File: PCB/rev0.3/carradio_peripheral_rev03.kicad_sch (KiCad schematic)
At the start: 258 parts, among them J1 ISO 10487 A (via pigtail), J10 Expansion, J11 SMA GNSS antenna, J12 Display buttons, J13 HDMI in (from VIM3), J14 Display FPC 40P 0.5mm, J17 RTL-SDR (internal), J18 VIM3 VIN (JST-XH 2P), J19 External USB 1, J2 VIM3 40-pin via 2x20 IDC ribb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, J20 External USB 2, J21 Expansion 2, J22 SWD, J5 VIM3 POWER key lead, J7 BH1750 light sensor, J8 ISO 10487 C1 (via pigtail), Q1 AO3400A, Q10 P-MOSFET -40V, Q11 CSD18543Q3A, Q12 CSD18543Q3A, Q2 P-MOSFET -60V, Q3 2N7002, SW1 BOOTSEL, SW2 RESET, U1 TPS560430XDBVR, U10 PCM5102APWR, U11 PCM5102APWR, U12 TPS55288RPMR, U13 CH334R, U14 CH334R, U15 LMR33630ADDA, U16 TPS2561DRCR, U17 USBLC6-2SC6, U18 USBLC6-2SC6, U19 AP2112K-3.3, U2 EL817S1(C), U20 RP2350B, U21 W25Q128JVS, U3 EL817S1(C), U4 EL817S1(C), U5 EL817S1(C), U6 LP5907MFX-3.3, U7 NEO-M9N-00B, U8 LP5907MFX-3.3, U9 LP5907MFX-3.3, Y1 12MHz, Y2 12MHz, Y3 12MHz

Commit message: PCB rev 0.3: KiCad import notes, TL3342 footprint for SW1/SW2
Checked every footprint name against the KiCad libraries and wrote down
the three parts that still need a footprint (TPS55288, fuse holder,
XUNPU FPC) and how to get them.

Co-Authored-By: Claude Opus 5.5 (1M context) <noreply@anthropic.com>
Claude-Session: https://claude.ai/code/session_01C8m2AkFwQrNE2yN9Ymgjwu
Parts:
- SW1, SW2: footprint (none) -> Button_Switch_SMD:SW_SPST_TL3342; MPN E-Switch TL3342F160QG (use the LCSC footprint; LCSC lists 5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 -> E-Switch TL3342F160QG
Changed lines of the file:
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@@
     (property
       "Footprint"
-      ""
+      "Button_Switch_SMD:SW_SPST_TL3342"
       (at 940 290 0)
       (effects
@@
     (property
       "MPN"
-      "E-Switch TL3342F160QG (use the LCSC footprint; LCSC lists 5.2x5.2mm)"
+      "E-Switch TL3342F160QG"
       (at 940 290 0)
       (effects
@@
     (property
       "Footprint"
-      ""
+      "Button_Switch_SMD:SW_SPST_TL3342"
       (at 1110 100 0)
       (effects
@@
     (property
       "MPN"
-      "E-Switch TL3342F160QG (use the LCSC footprint; LCSC lists 5.2x5.2mm)"
+      "E-Switch TL3342F160QG"
       (at 1110 100 0)
       (effects

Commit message: PCB rev 0.2/0.3: fix KiCad 10 footprint pad mismatches
- J13 HDMI footprint lives in Connector_Video, not Connector_HDMI
- USB-A shield pin renumbered SH to match the Molex 67643 footprint
- Hub crystals Y1/Y2 use Crystal_GND24 (pads 2/4 to GND)
- J14 FPC mounting pads (MP) tied to GND

Co-Authored-By: Claude Opus 5.5 (1M context) <noreply@anthropic.com>
Claude-Session: https://claude.ai/code/session_01C8m2AkFwQrNE2yN9Ymgjwu
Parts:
- removed J14: Display FPC 40P 0.5mm, Connector_FFC-FPC:Hirose_FH12-40S-0.5SH_1x40-1MP_P0.50mm_Horizontal, symbol Connector_Generic:Conn_01x40
- removed R84: 27Ω, Resistor_SMD:R_0603_1608Metric, symbol Device:R
- removed R87, R88, R89: 10k, Resistor_SMD:R_0603_1608Metric, symbol Device:R
- removed U19: AP2112K-3.3, Package_TO_SOT_SMD:SOT-23-5, symbol Regulator_Linear:AP2112K-3.3
- removed Y1, Y2: 12MHz, Crystal:Crystal_SMD_3225-4Pin_3.2x2.5mm, symbol Device:Crystal
- added C61: 1uF, Capacitor_SMD:C_0603_1608Metric, symbol Device:C
- added C81: 10uF, Capacitor_SMD:C_0805_2012Metric, symbol Device:C
- added J14: Display FPC 40P 0.5mm, Connector_FFC-FPC:Hirose_FH12-40S-0.5SH_1x40-1MP_P0.50mm_Horizontal, symbol Connector_Generic_MountingPin:Conn_01x40_MountingPin
- added J19: External USB 1, Connector_USB:USB_A_Molex_67643_Horizontal, symbol Connector:USB_A
- added R79: 1k, Resistor_SMD:R_0603_1608Metric, symbol Device:R
- added R85, R91, R92: 10k, Resistor_SMD:R_0603_1608Metric, symbol Device:R
- C76: renamed from J19; value External USB 1 -> 10uF; footprint Connector_USB:USB_A_Molex_67643_Horizontal -> Capacitor_SMD:C_0805_2012Metric; symbol Connector:USB_A -> Device:C; LCSC C2798029 -> C15850; MPN Molex 67643-0910 USB-A -> 0805 10uF 25V X5R
- J13: footprint Connector_HDMI:HDMI_A_Amphenol_10029449-x01xLF_Horizontal -> Connector_Video:HDMI_A_Amphenol_10029449-x01xLF_Horizontal
- R84: renamed from R85; value 10k -> 27Ω; LCSC C25804 -> C25190; MPN 0603 10k 1% -> UNI-ROYAL 0603WAF270JT5E 27R
- R87: renamed from R90; value 1k -> 10k; LCSC C21190 -> C25804; MPN 0603 1k 1% -> 0603 10k 1%
- R88: renamed from R79; value 1k -> 10k; LCSC C21190 -> C25804; MPN 0603 1k 1% -> 0603 10k 1%
- R90: renamed from R92; value 10k -> 1k; LCSC C25804 -> C21190; MPN 0603 10k 1% -> 0603 1k 1%
- U19: renamed from C81; value 10uF -> AP2112K-3.3; footprint Capacitor_SMD:C_0805_2012Metric -> Package_TO_SOT_SMD:SOT-23-5; symbol Device:C -> Regulator_Linear:AP2112K-3.3; LCSC C15850 -> C51118; MPN 0805 10uF 25V X5R -> Diodes AP2112K-3.3TRG1
- Y1: renamed from C61; value 1uF -> 12MHz; footprint Capacitor_SMD:C_0603_1608Metric -> Crystal:Crystal_SMD_3225-4Pin_3.2x2.5mm; symbol Device:C -> Device:Crystal_GND24; LCSC C77386 -> C9002; MPN 0603 1uF 50V X5R (Murata GRM188R61H105KAALD) -> YXC X322512MSB4SI 12MHz
- Y2: renamed from C76; value 10uF -> 12MHz; footprint Capacitor_SMD:C_0805_2012Metric -> Crystal:Crystal_SMD_3225-4Pin_3.2x2.5mm; symbol Device:C -> Device:Crystal_GND24; LCSC C15850 -> C9002; MPN 0805 10uF 25V X5R -> YXC X322512MSB4SI 12MHz
- renumbered R91 to R89
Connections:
- net +3V3_MCU: now also R87.1, R88.1, R89.1, U19.5 (VOUT), C81.1, R85.1; no longer R84.1, U19.1
- net +5V_AON: now also U19.1 (VIN), U19.3 (EN)
- net +5V_SYS: now also C61.1, J14.4 (Pin_4), J14.5 (Pin_5), J14.6 (Pin_6), R91.1; no longer R89.1, Y1.1
- net BL_EN: now also J14.37 (Pin_37)
- net BL_PWM: now also J14.36 (Pin_36)
- net EXT1_DM: now also J19.2 (D-); no longer C76.2 (D-)
- net EXT1_DP: now also J19.3 (D+); no longer C76.3 (D+)
- net EXT1_VBUS: now also J19.1 (VBUS); no longer C76.1 (VBUS)
- net GND: now also C76.2, J17.SH (Shield), J20.SH (Shield), Y1.4, Y2.4, C61.2, C81.2, J14.10 (Pin_10), J14.12 (Pin_12), J14.15 (Pin_15), J14.18 (Pin_18), J14.21 (Pin_21), J14.26 (Pin_26), J14.35 (Pin_35), J14.8 (Pin_8), J14.9 (Pin_9), J14.MP (MountPin), J19.4 (GND), J19.SH (Shield), R92.2; no longer C76.4 (GND), C76.5 (Shield), J17.5 (Shield), J20.5 (Shield), R90.2
- net GNSS_SAFEBOOT: now also R79.2; no longer R88.2
- net HDMI_5V: now also J14.27 (Pin_27)
- net HDMI_CEC: now also J14.23 (Pin_23)
- net HDMI_CLKN: now also J14.22 (Pin_22)
- net HDMI_CLKP: now also J14.20 (Pin_20)
- net HDMI_D0N: now also J14.19 (Pin_19)
- net HDMI_D0P: now also J14.17 (Pin_17)
- net HDMI_D1N: now also J14.16 (Pin_16)
- net HDMI_D1P: now also J14.14 (Pin_14)
- net HDMI_D2N: now also J14.13 (Pin_13)
- net HDMI_D2P: now also J14.11 (Pin_11)
- net HDMI_HPD: now also J14.28 (Pin_28)
- net HDMI_SCL: now also J14.24 (Pin_24)
- net HDMI_SDA: now also J14.25 (Pin_25)
- net HUB1_RST: now also R90.2; no longer R87.2
- net HUB2_3V3: now also C76.1; no longer Y2.1
- net HUB2_XI: now also Y2.1
- net HUB2_XO: now also Y2.3
- net HUB_XI: now also Y1.1
- net HUB_XO: now also Y1.3
- net MCU_5VSYS_ADC: now also R91.2, R92.1; no longer R89.2, R90.1
- net MCU_GNSS_SAFEBOOT: now also R79.1; no longer R88.1
- net MCU_HUB_RST: now also R90.1; no longer R87.1
- net MCU_RUN: now also R85.2; no longer R84.2
- net MCU_USBP_FAULT1: now also R87.2
- net MCU_USBP_FAULT2: now also R88.2
- net MCU_USBP_PG: now also R89.2
- net MCU_USB_DP: now also R84.2
- net MCU_USB_DP_R: now also R84.1
- net TOUCH_DN: now also J14.34 (Pin_34)
- net TOUCH_DP: now also J14.33 (Pin_33)
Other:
- moved on the sheet: R84, R87, R88, R89, R90

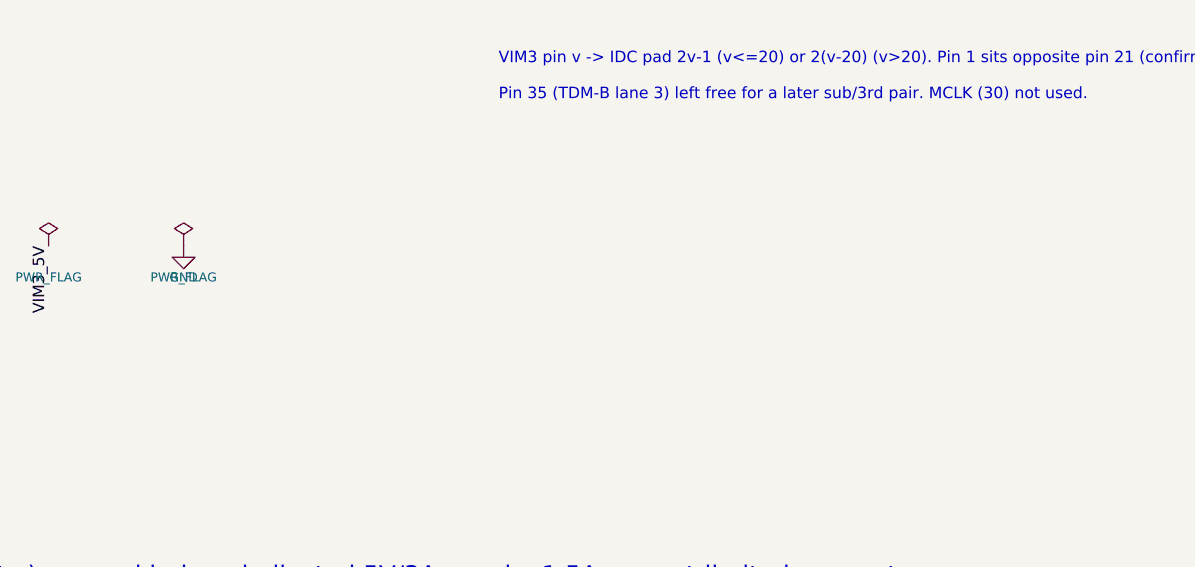
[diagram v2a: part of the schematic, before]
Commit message: PCB rev 0.3: board placement, HDMI routing, LCSC footprints
- carradio_peripheral_rev03.kicad_pcb: 109 x 92 mm, 4 layers (In1 GND plane),
  all 258 parts placed, 40-pin VIM3 header on the top edge
- HDMI socket -> display FPC routed; all 8 TMDS lines 40.25 mm (no skew)
- Every SMD ground pad has its own via to the GND plane
- carradio.pretty: TPS55288, Littelfuse 01530008Z and XUNPU FPC footprints
  from LCSC (J14 pads numbered by panel pin), registered via fp-lib-table
- Net classes and design rules in the project file; layout/ holds the
  scripts that generate the board
- Schematic: PWR_FLAGs added; KiCad 10 ERC shows only the two TPS2561
  output warnings

Co-Authored-By: Claude Opus 5.5 (1M context) <noreply@anthropic.com>
Claude-Session: https://claude.ai/code/session_01C8m2AkFwQrNE2yN9Ymgjwu
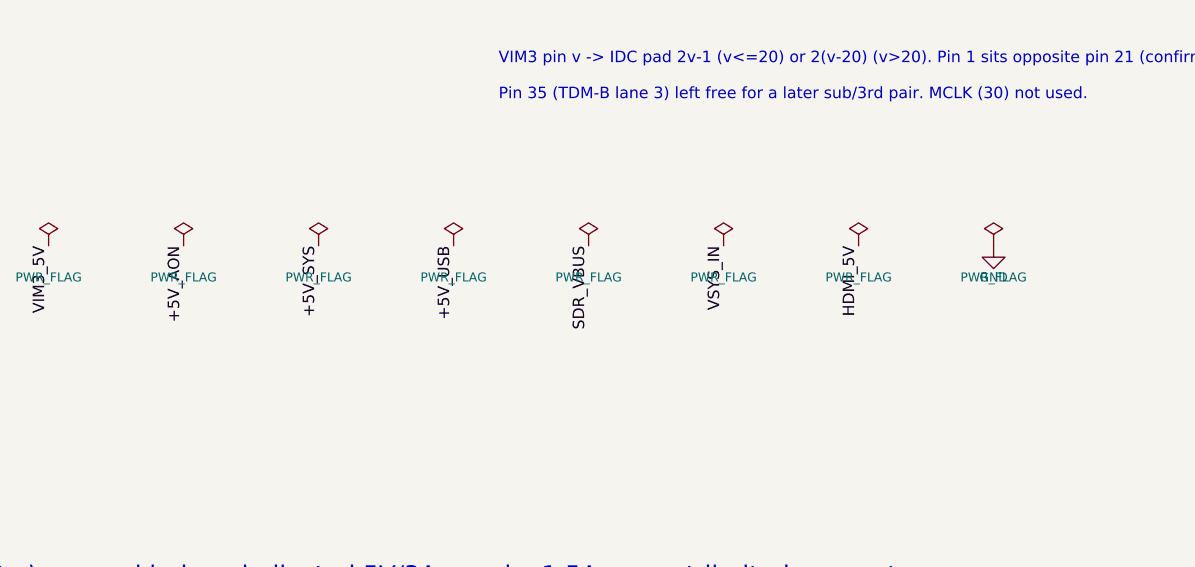
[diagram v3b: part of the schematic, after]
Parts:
- F4: footprint (none) -> carradio:Littelfuse_01530008Z; MPN Littelfuse 01530008Z mini blade holder (use the LCSC footpr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 -> Littelfuse 01530008Z mini blade holder + fuse C178942 Litte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
- J14: footprint Connector_FFC-FPC:Hirose_FH12-40S-0.5SH_1x40-1MP_P0.50mm_Horizontal -> carradio:XUNPU_FPC-05FB-40PH20; MPN XUNPU FPC-05FB-40PH20, 40P 0.5mm dual-contact flip-top 2.0mm (use the LCSC footprint, not FH12) -> XUNPU FPC-05FB-40PH20, 40P 0.5mm dual-contact flip-top 2.0mm (pads numbered by panel pin: pin 1 on the right, ribbon leaving the edge)
- U12: footprint (none) -> carradio:TPS55288RPMR_VQFN-HR-26; MPN TI TPS55288RPMR 36V buck-boost, I2C (footprint: use the Eas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 -> TI TPS55288RPMR

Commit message: PCB rev 0.3: rework TPS55288 area per TI layout guide (SLVAER0C)
- Schematic: net ties NT1/NT2 give ISP/ISN Kelvin taps at R74; NT3 joins
  a new analog ground (BB_AGND: U12 pins 7/10, R67-R70, C54, C55) to GND
  at the VCC cap. BOM unchanged.
- Layout: VCC cap at pin 19, BOOT caps on F.Cu without vias, control
  parts in a row beside U12 on an AGND pour, ISP/ISN routed as a pair.
  Displaced nets re-routed. DRC: 0 unconnected, no copper or courtyard
  errors.
- TPS55288_LAYOUT_REVIEW.md lists what changed and what was left.

Co-Authored-By: Claude Opus 5.5 (1M context) <noreply@anthropic.com>
Claude-Session: https://claude.ai/code/session_01C8m2AkFwQrNE2yN9Ymgjwu
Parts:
- removed F5: PTC 0.5A, Fuse:Fuse_1206_3216Metric, symbol Device:Polyfuse
- removed J22: SWD, Connector_PinHeader_2.54mm:PinHeader_1x04_P2.54mm_Vertical, symbol Connector_Generic:Conn_01x04
- removed Q11: CSD18543Q3A, Package_SON:VSON-8_3.3x3.3mm_P0.65mm_NexFET, symbol Transistor_FET:CSD18543Q3A
- removed R71: 8.2k, Resistor_SMD:R_0603_1608Metric, symbol Device:R
- removed SW1: BOOTSEL, Button_Switch_SMD:SW_SPST_TL3342, symbol Switch:SW_Push
- added J17: RTL-SDR (internal), Connector_USB:USB_A_Molex_67643_Horizontal, symbol Connector:USB_A
- added NT1, NT2, NT3: NetTie, NetTie:NetTie-2_SMD_Pad0.5mm, symbol Device:NetTie_2
- added R70: 100k, Resistor_SMD:R_0603_1608Metric, symbol Device:R
- added R73: 1k, Resistor_SMD:R_0603_1608Metric, symbol Device:R
- added R85: 10k, Resistor_SMD:R_0603_1608Metric, symbol Device:R
- added Y3: 12MHz, Crystal:Crystal_SMD_3225-4Pin_3.2x2.5mm, symbol Device:Crystal_GND24
- F5: renamed from J17; value RTL-SDR (internal) -> PTC 0.5A; footprint Connector_USB:USB_A_Molex_67643_Horizontal -> Fuse:Fuse_1206_3216Metric; symbol Connector:USB_A -> Device:Polyfuse; LCSC C2798029 -> C75464; MPN Molex 67643-0910 USB-A -> Bourns MF-NSMF050-2
- J22: renamed from R85; value 10k -> SWD; footprint Resistor_SMD:R_0603_1608Metric -> Connector_PinHeader_2.54mm:PinHeader_1x04_P2.54mm_Vertical; symbol Device:R -> Connector_Generic:Conn_01x04; LCSC C25804 -> C124378; MPN 0603 10k 1% -> 1x4 male header 2.54mm
- Q11: renamed from R73; value 1k -> CSD18543Q3A; footprint Resistor_SMD:R_0603_1608Metric -> Package_SON:VSON-8_3.3x3.3mm_P0.65mm_NexFET; symbol Device:R -> Transistor_FET:CSD18543Q3A; LCSC C21190 -> C840100; MPN 0603 1k 1% -> TI CSD18543Q3A 60V 8.5mOhm N-MOSFET
- R71: renamed from R70; value 100k -> 8.2k; LCSC C25803 -> C25981; MPN 0603 100k 1% -> 0603 8.2k 1%
- SW1: renamed from Y3; value 12MHz -> BOOTSEL; footprint Crystal:Crystal_SMD_3225-4Pin_3.2x2.5mm -> Button_Switch_SMD:SW_SPST_TL3342; symbol Device:Crystal_GND24 -> Switch:SW_Push; LCSC C20625731 -> C2886898; MPN Abracon ABM8-272-T3 12MHz (Raspberry Pi reference part) -> E-Switch TL3342F160QG
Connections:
- net +3V3_MCU: now also R85.1; no longer J22.1
- net +5V_SYS: now also F5.1, NT2.2; no longer U12.13 (ISN)
- net BB_CDC: now also R70.1; no longer R71.1
- net BB_COMP: now also R71.1
- net BB_COMP_RC: now also R71.2
- net BB_DR1H: now also Q11.4 (G)
- net BB_SW1: now also Q11.1 (S), Q11.2 (S), Q11.3 (S)
- net BB_VOUT: now also NT1.2; no longer U12.12 (ISP)
- net BOOTSEL_SW: now also SW1.1
- net GND: now also J22.2 (Pin_2), J17.4 (GND), J17.SH (Shield), NT3.2, Y3.2, Y3.4; no longer C54.2, C55.2, F5.4 (GND), F5.SH (Shield), R67.2, R68.2, R69.2, R71.2, SW1.4, U12.10 (AGND), U12.7 (DITH/SYNC)
- net MCU_RUN: now also J22.4 (Pin_4), R85.2; no longer J22.2
- net MCU_SWCLK: now also J22.1 (Pin_1)
- net MCU_SWDIO: now also J22.3 (Pin_3)
- net MCU_VIM3_PWR_EN: now also R73.1; no longer Q11.1
- net MCU_XIN: now also Y3.1; no longer SW1.1
- net MCU_XTAL_R: now also Y3.3; no longer SW1.3
- net SDR_DM: now also J17.2 (D-); no longer F5.2 (D-)
- net SDR_DP: now also J17.3 (D+); no longer F5.3 (D+)
- net SDR_VBUS: now also F5.2, J17.1 (VBUS); no longer F5.1 (VBUS)
- net VIM3_PWR_EN: now also R73.2; no longer Q11.2
- net VSYS_IN: now also Q11.5 (D)
- new net BB_AGND: C54.2, C55.2, NT3.1, R67.2, R68.2, R69.2, R70.2, U12.10 (AGND), U12.7 (DITH/SYNC)
- new net BB_ISN: NT2.1, U12.13 (ISN)
- new net BB_ISP: NT1.1, U12.12 (ISP)
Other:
- moved on the sheet: R71

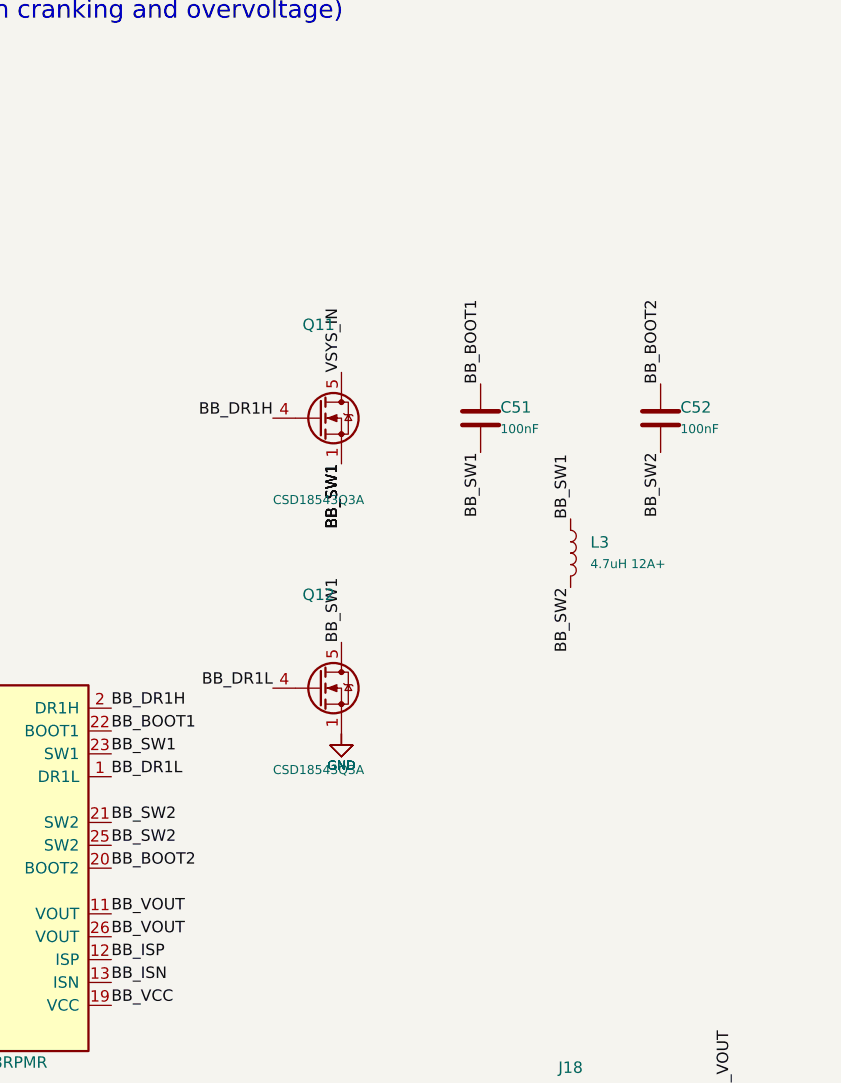
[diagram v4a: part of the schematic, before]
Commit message: PCB rev 0.3: TPS55288 gate resistors and SW1 snubber
Adds R97/R98 (0402, fitted as 0 ohm) in series with the DR1H and DR1L
gates and an RC snubber C104 (1nF) + R99 (2.2 ohm 0805) from SW1 to GND,
the two items the TI layout review left open. Schematic, BOM and board
updated; DRC 0 unconnected, no copper or courtyard errors.

Co-Authored-By: Claude Opus 5.5 (1M context) <noreply@anthropic.com>
Claude-Session: https://claude.ai/code/session_01C8m2AkFwQrNE2yN9Ymgjwu
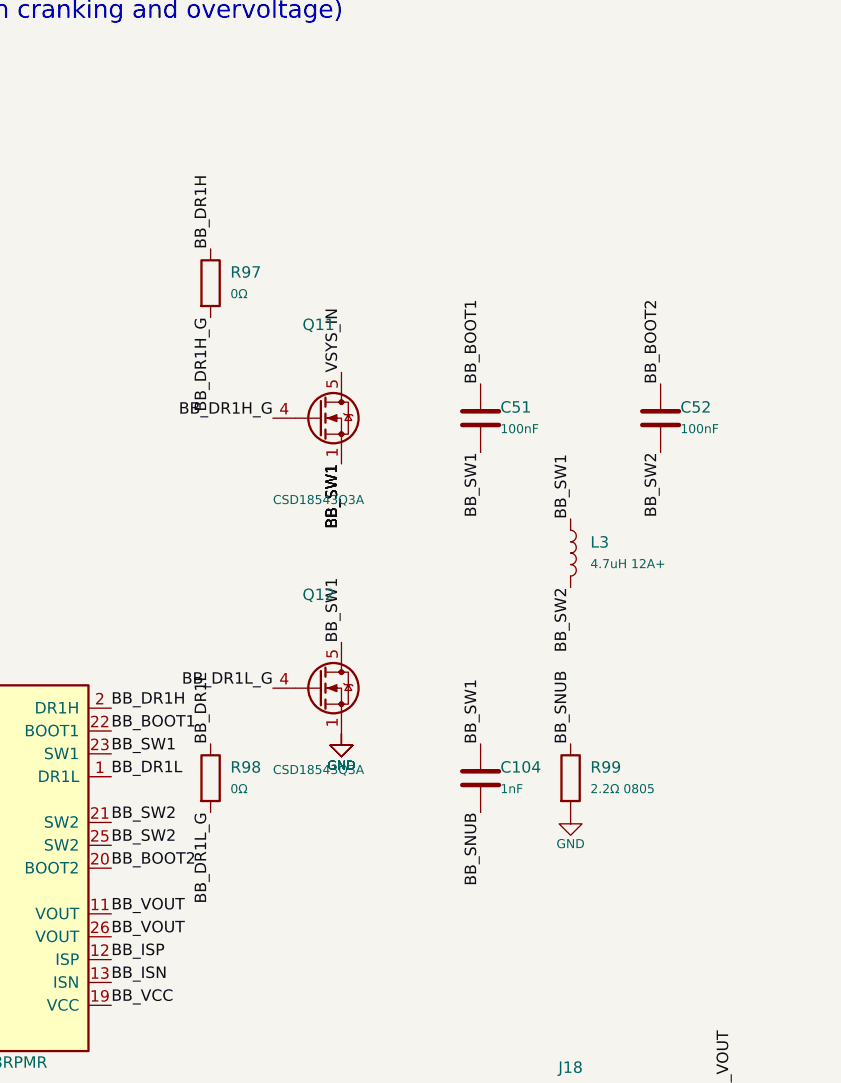
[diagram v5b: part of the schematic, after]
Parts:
- added C104: 1nF, Capacitor_SMD:C_0603_1608Metric, symbol Device:C
- added R97, R98: 0Ω, Resistor_SMD:R_0402_1005Metric, symbol Device:R
- added R99: 2.2Ω 0805, Resistor_SMD:R_0805_2012Metric, symbol Device:R
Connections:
- net BB_DR1H: now also R97.1; no longer Q11.4 (G)
- net BB_DR1L: now also R98.1; no longer Q12.4 (G)
- net BB_SW1: now also C104.1
- net GND: now also R99.2
- new net BB_DR1H_G: Q11.4 (G), R97.2
- new net BB_DR1L_G: Q12.4 (G), R98.2
- new net BB_SNUB: C104.2, R99.1
